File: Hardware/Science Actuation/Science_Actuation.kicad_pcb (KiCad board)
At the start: 2 copper layers, 120 parts, among them J4 RJ45_LED_Shielded, Q1 Si4156DY, Q10 Si4156DY, Q11 Si4156DY, Q12 Si4156DY, Q13 Si4156DY, Q14 Si4156DY, Q15 Si4156DY, Q16 Si4156DY, Q2 Si4156DY, Q3 Si4156DY, Q4 Si4156DY, Q5 Si4156DY, Q6 Si4156DY, Q7 Si4156DY, Q8 Si4156DY, Q9 Si4156DY, SW1 SW_Push, SW10 SW_SPDT, SW2 SW_Push, SW3 SW_Push, SW4 SW_Push, SW5 SW_Push, SW6 SW_Push, U1 Teensy4.1_DEV-16771, U10 IRS2308, U11 IRS2308, U12 74LVC2G04, U13 IRS2308, U14 IRS2308, U2 OKI, U3 74LVC2G04, U4 IRS2308, U5 IRS2308, U6 74LVC2G04, U7 IRS2308, U8 IRS2308, U9 74LVC2G04

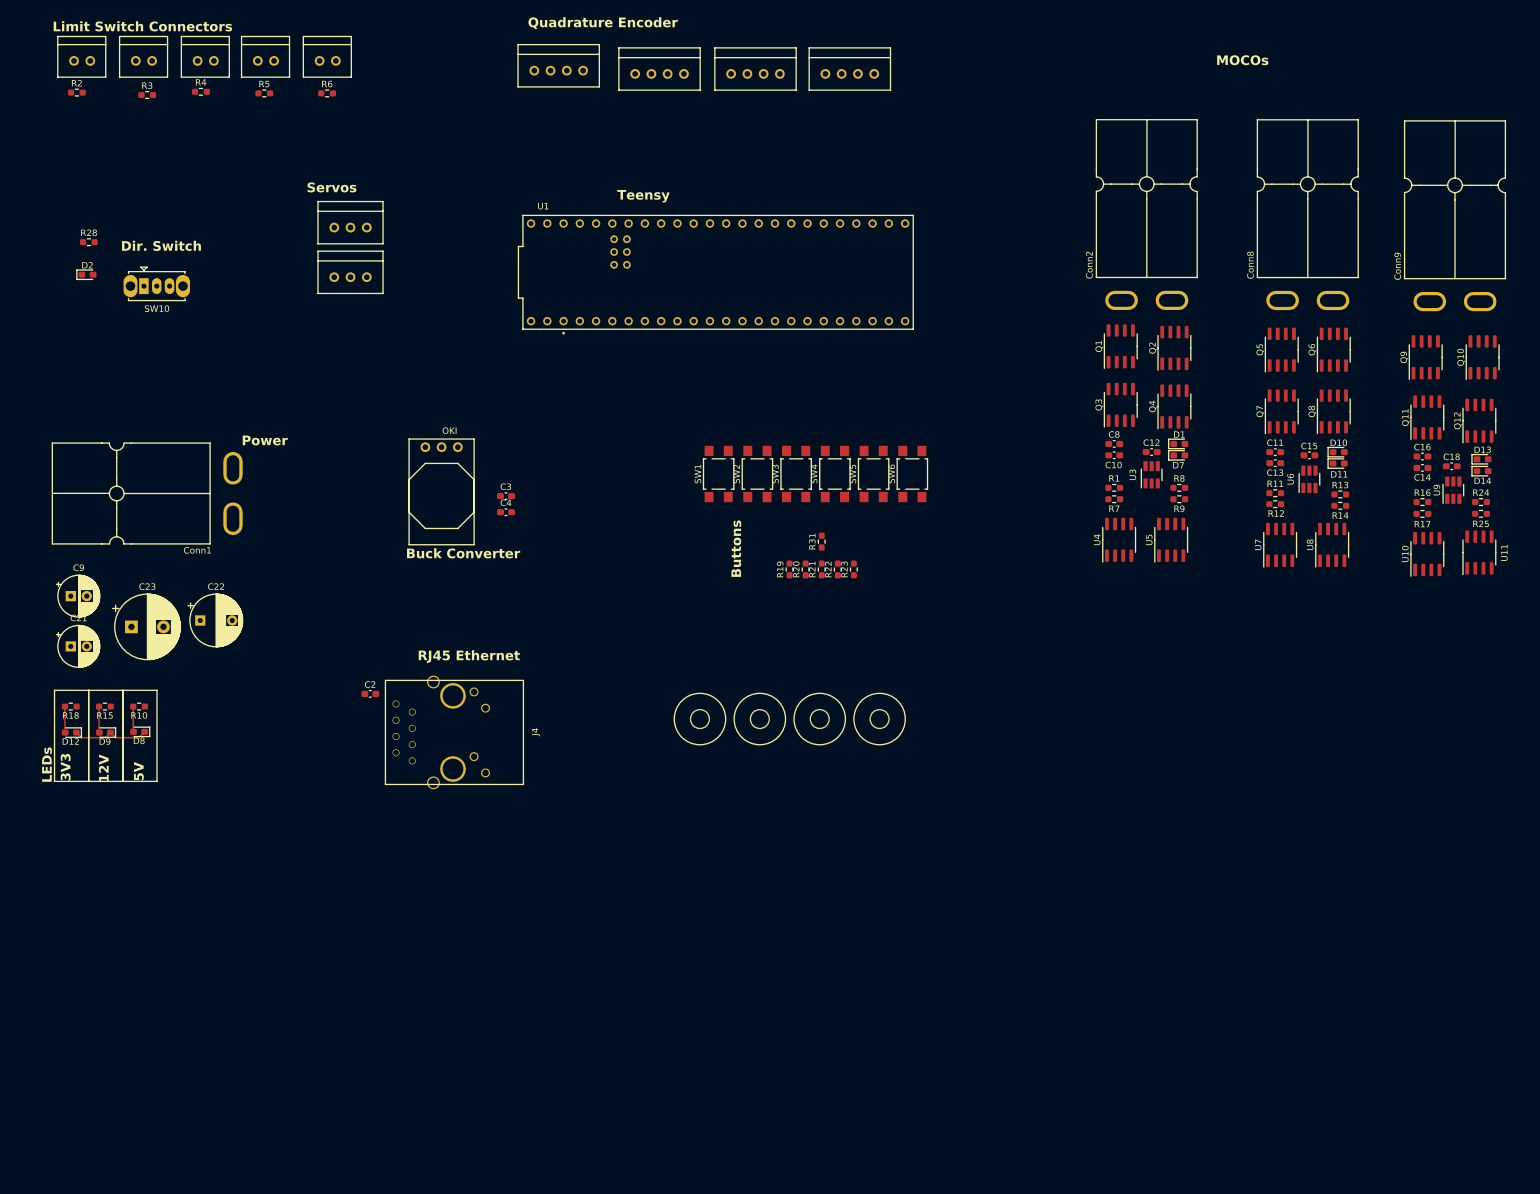
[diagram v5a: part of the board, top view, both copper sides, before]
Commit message: Started connecting traces and positioning components of PCB
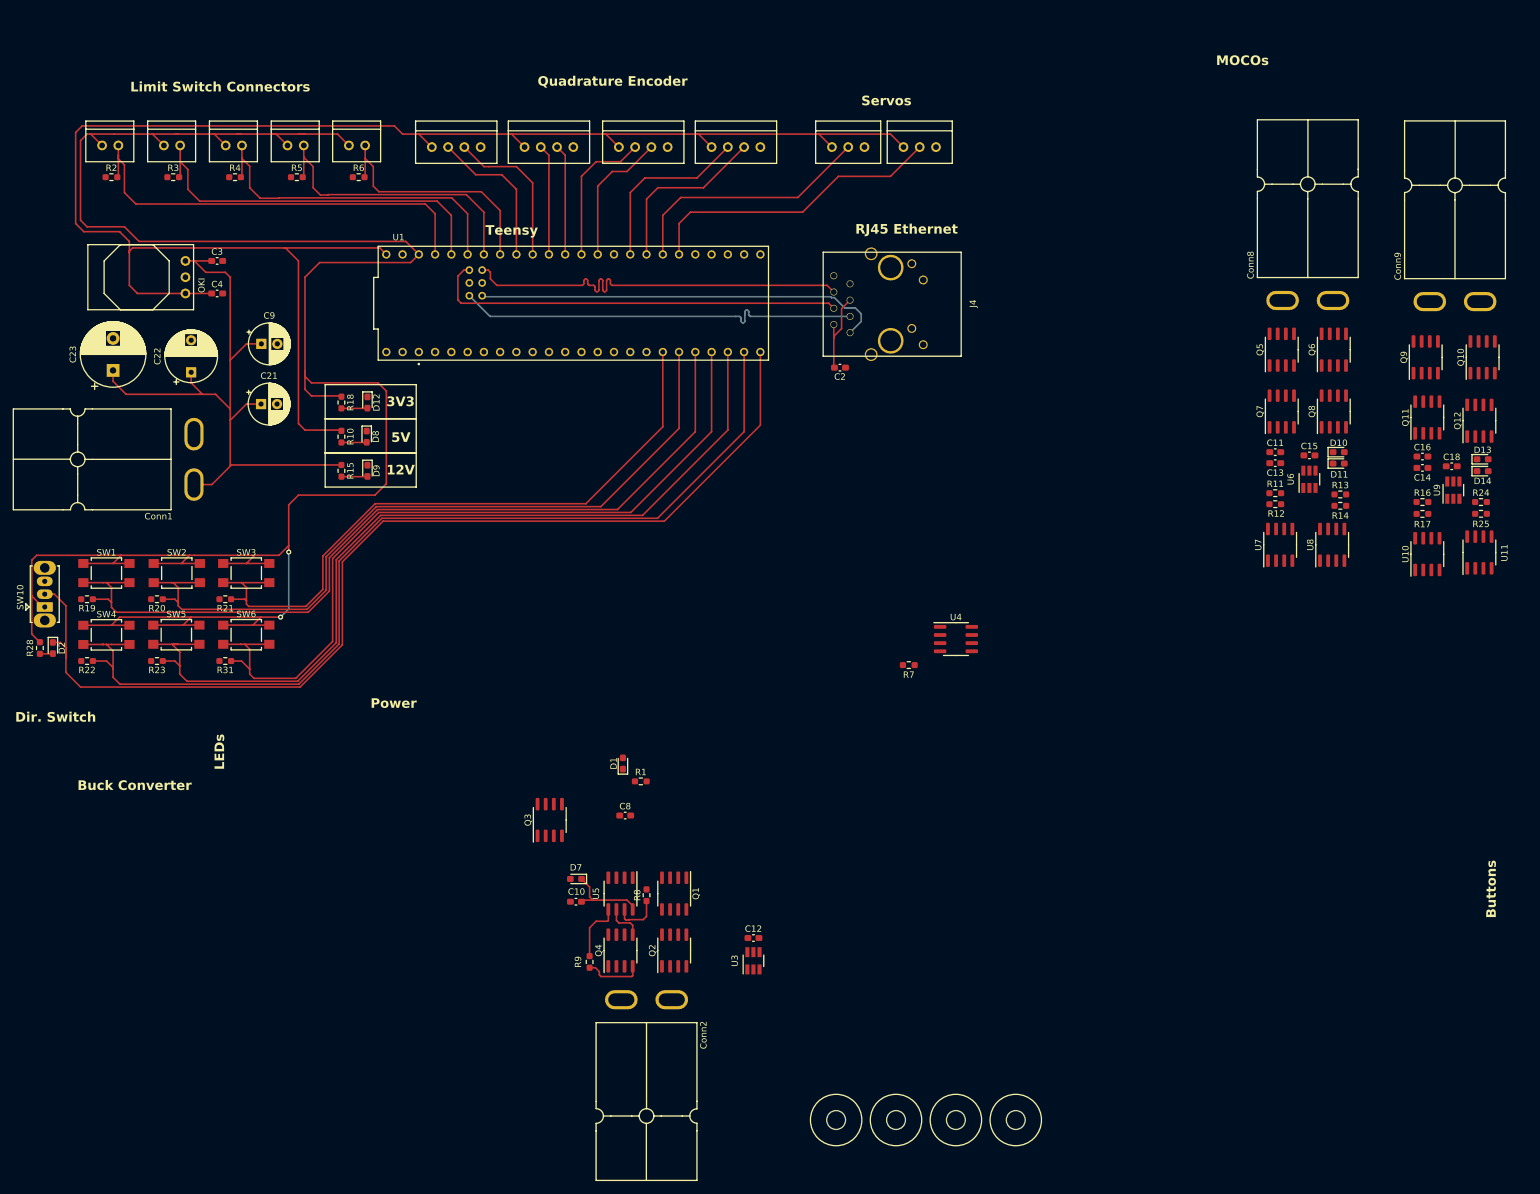
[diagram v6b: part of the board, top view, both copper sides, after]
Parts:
- moved Conn2 139.1 mm to (104.5, 167.1), turned to 90 degrees
- moved Q2 122.3 mm to (113.3, 159.8)
- moved Q4 121.3 mm to (104.9, 159.8)
- moved R22 118.1 mm to (21.6, 114.6), turned to 180 degrees
- moved R9 117.1 mm to (100.1, 161.5), turned to -90 degrees
- moved SW4 116.5 mm to (24.6, 110.5), turned to 0 degrees
- moved D7 115.1 mm to (97.9, 148.6), turned to 180 degrees
- moved SW5 111.8 mm to (35.5, 110.4), turned to 0 degrees
- moved Q1 110.3 mm to (113.3, 150.9), turned to -90 degrees
- moved Q3 110.3 mm to (93.9, 139.4)
- moved R19 109.8 mm to (21.6, 104.9), turned to 180 degrees
- moved R23 109.8 mm to (32.5, 114.6), turned to 180 degrees
- moved C10 109.2 mm to (97.9, 152.1), turned to 180 degrees
- moved SW6 107.0 mm to (46.5, 110.4), turned to 0 degrees
- moved R8 104.7 mm to (109.0, 151.1), turned to 90 degrees
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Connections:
- QuadEncode1 pad 2: Encoder_1a -> Encoder_2a
- QuadEncode1 pad 3: Encoder_1b -> Encoder_2b
- QuadEncode2 pad 2: Encoder_1a -> Encoder_3a
- QuadEncode2 pad 3: Encoder_1b -> Encoder_3b
- QuadEncode3 pad 2: Encoder_1a -> Encoder_4a
- QuadEncode3 pad 3: Encoder_1b -> Encoder_4b
- Servo1 pad 2: Servo_1 -> Servo_2
- Servo2 pad 2: Servo_2 -> Servo_1
- U1 pad 0: LimitSwitch5 -> unconnected-(U1-RX1-Pad0)
- U1 pad 1: LimitSwitch4 -> unconnected-(U1-TX1-Pad1)
- U1 pad 13: unconnected-(U1-SCK-Pad13) -> Encoder_3b
- U1 pad 14: Encoder_1b -> Encoder_3a
- U1 pad 15: unconnected-(U1-A1-Pad15) -> Encoder_2b
- U1 pad 16: unconnected-(U1-A2-Pad16) -> Encoder_2a
- U1 pad 17: unconnected-(U1-A3-Pad17) -> Encoder_1b
- U1 pad 18: unconnected-(U1-A4-Pad18) -> Encoder_1a
- U1 pad 19: unconnected-(U1-A5-Pad19) -> LimitSwitch5
- U1 pad 2: LimitSwitch3 -> unconnected-(U1-OUT2-Pad2)
- U1 pad 20: unconnected-(U1-A6-Pad20) -> LimitSwitch4
- U1 pad 21: LimitSwitch1 -> LimitSwitch3
- U1 pad 22: unconnected-(U1-A8-Pad22) -> LimitSwitch2
- U1 pad 23: LimitSwitch2 -> LimitSwitch1
- U1 pad 24: SW1 -> unconnected-(U1-A10-Pad24)
- U1 pad 25: SW2 -> unconnected-(U1-A11-Pad25)
- U1 pad 27: SW4 -> SW2
- U1 pad 28: SW5 -> SW1
- U1 pad 30: unconnected-(U1-CRX3-Pad30) -> SW5
- U1 pad 31: DIR_SW -> SW4
- U1 pad 33: Servo_2 -> unconnected-(U1-MCLK2-Pad33)
- U1 pad 34: Encoder_4a -> unconnected-(U1-RX8-Pad34)
- U1 pad 35: Encoder_4b -> unconnected-(U1-TX8-Pad35)
- U1 pad 36: Servo_1 -> unconnected-(U1-CS2-Pad36)
- U1 pad 37: Encoder_3a -> unconnected-(U1-CS3-Pad37)
- U1 pad 38: Encoder_3b -> Servo_2
- U1 pad 39: Encoder_2a -> Servo_1
- U1 pad 40: Encoder_2b -> Encoder_4b
- U1 pad 41: Encoder_1a -> Encoder_4a
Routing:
- net +3V3: track 0.00 -> 366.9 mm, vias 0 -> 2
- net +5V: track 0.00 -> 267.9 mm
- net DIR_SW: track 0.00 -> 163.8 mm
- net SW4: track 0.00 -> 152.0 mm
- net SW5: track 0.00 -> 138.3 mm
- net SW1: track 0.00 -> 133.2 mm
- net SW6: track 0.00 -> 124.2 mm
- net SW2: track 0.00 -> 118.9 mm
- net SW3: track 0.00 -> 104.9 mm
- net +12V: track 0.00 -> 102.3 mm
- net LimitSwitch1: track 0.00 -> 67.5 mm
- net R+: track 0.00 -> 65.2 mm
- net R-: track 0.00 -> 65.0 mm
- net T+: track 0.00 -> 64.0 mm
- net T-: track 0.00 -> 63.9 mm
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
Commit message: lots of layout things; got a pretty solid layout for the moco circuits; still needs a decent bit of cleanup, trace routing, via stitching, etc.
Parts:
- removed R19, R20, R21, R22, R23, R31: 4700, Resistor_SMD:R_0603_1608Metric_Pad0.98x0.95mm_HandSolder
- added C1: 10uF, Capacitor_SMD:C_0603_1608Metric_Pad1.08x0.95mm_HandSolder, F.Cu at (36.7, -5.08)
- added C5: 10uF, Capacitor_SMD:C_0603_1608Metric_Pad1.08x0.95mm_HandSolder, F.Cu at (36.7, 31.6)
- added C6: 10uF, Capacitor_SMD:C_0603_1608Metric_Pad1.08x0.95mm_HandSolder, F.Cu at (36.7, 4.83)
- added C7: 10uF, Capacitor_SMD:C_0603_1608Metric_Pad1.08x0.95mm_HandSolder, F.Cu at (36.7, 41.4)
- added Conn11: Molex_SL_02, MRDT_Connectors:MOLEX_SL_02_Vertical, F.Cu at (76.9, 49.8)
- added R32: 4700, Resistor_SMD:R_0603_1608Metric_Pad0.98x0.95mm_HandSolder, F.Cu at (79.2, 45.9)
- Conn1, Conn10, Conn2, Conn8, Conn9: moved to B.Cu
- R10: value 620 -> 560
- R18: value 270 -> 300
- U2: value OKI -> OKI-78SR-5_1.5-W36H-C; footprint MRDT_Devices:OKI_Horizontal -> Converter_DCDC:Converter_DCDC_Murata_OKI-78SR_Horizontal
- moved Q15 272.1 mm to (6.52, -14.7), turned to 180 degrees
- moved H3 270.4 mm to (1.27, -27.7)
- moved Q13 261.8 mm to (6.52, -6.73), turned to 180 degrees
- moved R30 260.9 mm to (25.6, -15.5), turned to 180 degrees
- moved Conn10 257.6 mm to (13.4, -4.66), turned to 0 degrees
- moved R29 256.6 mm to (30.4, -17.5), turned to 180 degrees
- moved U14 255.8 mm to (31.8, -13.5), turned to 180 degrees
- moved Q14 253.8 mm to (19.5, -5.33), turned to 180 degrees
- moved R27 248.5 mm to (25.6, -7.75), turned to 180 degrees
- moved Q16 248.4 mm to (19.5, -13.2), turned to 180 degrees
- moved D16 247.7 mm to (34.7, -9.40)
- moved C19 247.0 mm to (26.6, -12.4), turned to 90 degrees
- moved U13 244.9 mm to (31.8, -5.08), turned to 180 degrees
- moved R26 244.0 mm to (30.4, -9.40), turned to 180 degrees
- moved D15 244.0 mm to (34.7, -1.02)
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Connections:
- C10 pad 2: /M- -> /M1-
- C11 pad 2: /M+ -> /M2+
- C13 pad 2: /M- -> /M2-
- C14 pad 2: /M+ -> /M3+
- C16 pad 2: /M- -> /M3-
- C17 pad 2: /M+ -> /M4+
- C19 pad 2: /M- -> /M4-
- C8 pad 2: /M+ -> /M1+
- Conn10 pad 1: /M+ -> /M4+
- Conn10 pad 2: /M- -> /M4-
- Conn2 pad 1: /M+ -> /M1+
- Conn2 pad 2: /M- -> /M1-
- Conn8 pad 1: /M+ -> /M2+
- Conn8 pad 2: /M- -> /M2-
- Conn9 pad 1: /M+ -> /M3+
- Conn9 pad 2: /M- -> /M3-
- Q1 pad 1: /M+ -> /M1+
- Q1 pad 2: /M+ -> /M1+
- Q1 pad 3: /M+ -> /M1+
- Q10 pad 5: /M+ -> /M3+
- Q10 pad 6: /M+ -> /M3+
- Q10 pad 7: /M+ -> /M3+
- Q10 pad 8: /M+ -> /M3+
- Q11 pad 1: /M- -> /M3-
- Q11 pad 2: /M- -> /M3-
- Q11 pad 3: /M- -> /M3-
- Q12 pad 5: /M- -> /M3-
- Q12 pad 6: /M- -> /M3-
- Q12 pad 7: /M- -> /M3-
- Q12 pad 8: /M- -> /M3-
- Q13 pad 1: /M+ -> /M4+
- Q13 pad 2: /M+ -> /M4+
- Q13 pad 3: /M+ -> /M4+
- Q14 pad 5: /M+ -> /M4+
- Q14 pad 6: /M+ -> /M4+
- Q14 pad 7: /M+ -> /M4+
- Q14 pad 8: /M+ -> /M4+
- Q15 pad 1: /M- -> /M4-
- Q15 pad 2: /M- -> /M4-
- Q15 pad 3: /M- -> /M4-
- Q16 pad 5: /M- -> /M4-
- Q16 pad 6: /M- -> /M4-
- Q16 pad 7: /M- -> /M4-
- Q16 pad 8: /M- -> /M4-
- Q2 pad 5: /M+ -> /M1+
- Q2 pad 6: /M+ -> /M1+
- Q2 pad 7: /M+ -> /M1+
- Q2 pad 8: /M+ -> /M1+
- Q3 pad 1: /M- -> /M1-
- Q3 pad 2: /M- -> /M1-
- Q3 pad 3: /M- -> /M1-
- Q4 pad 5: /M- -> /M1-
- Q4 pad 6: /M- -> /M1-
- Q4 pad 7: /M- -> /M1-
- Q4 pad 8: /M- -> /M1-
- Q5 pad 1: /M+ -> /M2+
- Q5 pad 2: /M+ -> /M2+
- Q5 pad 3: /M+ -> /M2+
- Q6 pad 5: /M+ -> /M2+
- Q6 pad 6: /M+ -> /M2+
- Q6 pad 7: /M+ -> /M2+
- Q6 pad 8: /M+ -> /M2+
- Q7 pad 1: /M- -> /M2-
- Q7 pad 2: /M- -> /M2-
- Q7 pad 3: /M- -> /M2-
- Q8 pad 5: /M- -> /M2-
- Q8 pad 6: /M- -> /M2-
- Q8 pad 7: /M- -> /M2-
- Q8 pad 8: /M- -> /M2-
- Q9 pad 1: /M+ -> /M3+
- Q9 pad 2: /M+ -> /M3+
- Q9 pad 3: /M+ -> /M3+
- SW1 pad 1: +3V3 -> SW1
- SW1 pad 2: SW1 -> GND
- SW2 pad 1: +3V3 -> SW2
- SW2 pad 2: SW2 -> GND
- SW3 pad 1: +3V3 -> SW3
- SW3 pad 2: SW3 -> GND
- SW4 pad 1: +3V3 -> SW4
- SW4 pad 2: SW4 -> GND
- SW5 pad 1: +3V3 -> SW5
- SW5 pad 2: SW5 -> GND
- SW6 pad 1: +3V3 -> SW6
- SW6 pad 2: SW6 -> GND
- U1 pad 0: unconnected-(U1-RX1-Pad0) -> SW2
- U1 pad 1: unconnected-(U1-TX1-Pad1) -> SW4
- U1 pad 10: MOCO1_RVS -> MOCO3_RVS
- U1 pad 11: MOCO2_FWD -> MOCO3_FWD
- U1 pad 12: MOCO2_RVS -> unconnected-(U1-MISO-Pad12)
- U1 pad 2: unconnected-(U1-OUT2-Pad2) -> SW1
- U1 pad 26: SW3 -> unconnected-(U1-A12-Pad26)
- U1 pad 27: SW2 -> unconnected-(U1-A13-Pad27)
- U1 pad 28: SW1 -> unconnected-(U1-RX7-Pad28)
- U1 pad 29: SW6 -> unconnected-(U1-TX7-Pad29)
- U1 pad 3: MOCO3_FWD -> SW5
- U1 pad 30: SW5 -> unconnected-(U1-CRX3-Pad30)
- U1 pad 31: SW4 -> MOCO1_RVS
- U1 pad 32: DIR_SW -> MOCO1_FWD
- U1 pad 4: MOCO3_RVS -> SW3
- U1 pad 5: MOCO4_FWD -> SW6
- U1 pad 6: MOCO4_RVS -> MOCO4_FWD
- U1 pad 7: unconnected-(U1-RX2-Pad7) -> MOCO4_RVS
- U1 pad 8: unconnected-(U1-TX2-Pad8) -> MOCO2_RVS
- U1 pad 9: MOCO1_FWD -> MOCO2_FWD
- U10 pad 6: /M+ -> /M3+
- U11 pad 6: /M- -> /M3-
- U13 pad 6: /M+ -> /M4+
- U14 pad 6: /M- -> /M4-
- U4 pad 6: /M+ -> /M1+
- U5 pad 6: /M- -> /M1-
- U7 pad 6: /M+ -> /M2+
- U8 pad 6: /M- -> /M2-
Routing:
- net +3V3: track 366.9 -> 18.6 mm
- net +5V: track 267.9 -> 3.08 mm
- net DIR_SW: track 163.8 -> 0.00 mm
- net +12V: track 102.3 -> 255.7 mm, vias 0 -> 8
- net SW4: track 152.0 -> 25.0 mm
- net SW5: track 138.3 -> 19.3 mm
- net SW2: track 118.9 -> 14.2 mm
- net SW1: track 133.2 -> 35.7 mm
- net SW6: track 124.2 -> 38.9 mm
- net SW3: track 104.9 -> 28.2 mm
- net LimitSwitch1: track 67.5 -> 0.00 mm
- net R+: track 65.2 -> 0.00 mm
- net R-: track 65.0 -> 0.00 mm
- net T+: track 64.0 -> 0.00 mm
- net T-: track 63.9 -> 0.00 mm
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- added copper zone on B.Cu, net +12V
- added copper zone on F.Cu, net +12V
- added copper zone on F.Cu, net /M1+
- added copper zone on F.Cu, net /M1-
- added copper zone on F.Cu, net /M2-
- added copper zone on F.Cu, net /M3+
- added copper zone on F.Cu, net /M3-
- added copper zone on F.Cu, net /M4+
- added copper zone on F.Cu, net /M4-
- added copper zone on B.Cu, net GND
- added copper zone on F.Cu, net GND
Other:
- board outline added: 90.4 x 109.5 mm
- board text removed: "Buck Converter"
- board text removed: "Buttons"
- board text removed: "Dir. Switch"
- board text removed: "LEDs"
- board text removed: "Limit Switch Connectors"
- board text removed: "MOCOs"
- board text removed: "Power"
- board text removed: "Quadrature Encoder"
- board text removed: "RJ45 Ethernet"
- board text removed: "Servos"
- board text removed: "Teensy"

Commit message: more routing and shtuff
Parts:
- moved SW10 4.08 mm to (69.4, -15.1), turned to 0 degrees
- moved D2 2.03 mm to (73.4, -9.65)
- moved R28 2.03 mm to (71.4, -9.65)
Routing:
- net +5V: track 3.08 -> 302.8 mm, vias 0 -> 7
- net +3V3: track 18.6 -> 166.8 mm, vias 2 -> 12
- net +12V: track 255.7 -> 268.8 mm
- net /M3+: track 16.7 -> 20.6 mm
- net MOCO1_FWD: track 22.4 -> 26.1 mm, vias 2 -> 3
- net SW2: track 14.2 -> 17.1 mm, vias 0 -> 2
- net MOCO3_RVS: track 25.0 -> 27.8 mm, vias 2 -> 3
- net MOCO2_FWD: track 21.8 -> 24.1 mm
- net SW4: track 25.0 -> 27.3 mm, vias 0 -> 2
- net SW1: track 35.7 -> 37.7 mm, vias 0 -> 2
- net /M4-: track 16.1 -> 17.8 mm
- net MOCO3_FWD: track 31.9 -> 33.5 mm, vias 2 -> 3
- net SW3: track 28.2 -> 29.6 mm, vias 0 -> 2
- net Net-(U4-LIN): track 12.4 -> 13.6 mm
- net /M1+: track 16.4 -> 17.6 mm
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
